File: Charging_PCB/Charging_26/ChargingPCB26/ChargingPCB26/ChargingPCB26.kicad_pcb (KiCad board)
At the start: 2 copper layers, 100 x 100 mm, 61 parts, among them J1 Molex6pin, J2 Molex6pin, K101 Relay_SPDT_Omron_G2RL-1, K102 Relay_SPDT_Omron_G2RL-1, Q1 Q_NMOS_GDS, Q103 Q_NPN_BEC, Q104 Q_NPN_BEC, Q105 Q_NPN_BEC, Q106 Q_NPN_BEC, Q2 Q_NMOS_GDS, Q3 Q_NMOS_GDS, Q4 Q_NMOS_GDS, SW101 SW_Omron_B3FS, SW102 SW_Omron_B3FS, U1 SFH617A-1, U107 LM7805_TO220, U2 SFH617A-1, U5 74LS279, U6 74HC00

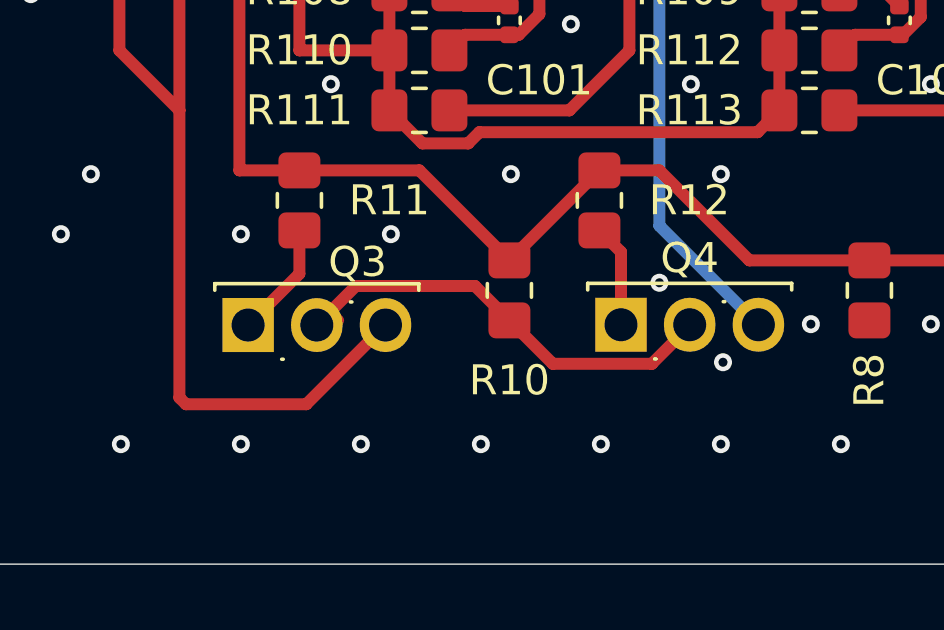
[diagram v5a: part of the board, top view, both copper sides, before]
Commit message: charging
fixed issue where Q3 and Q4 mosfets had source and drain swapped
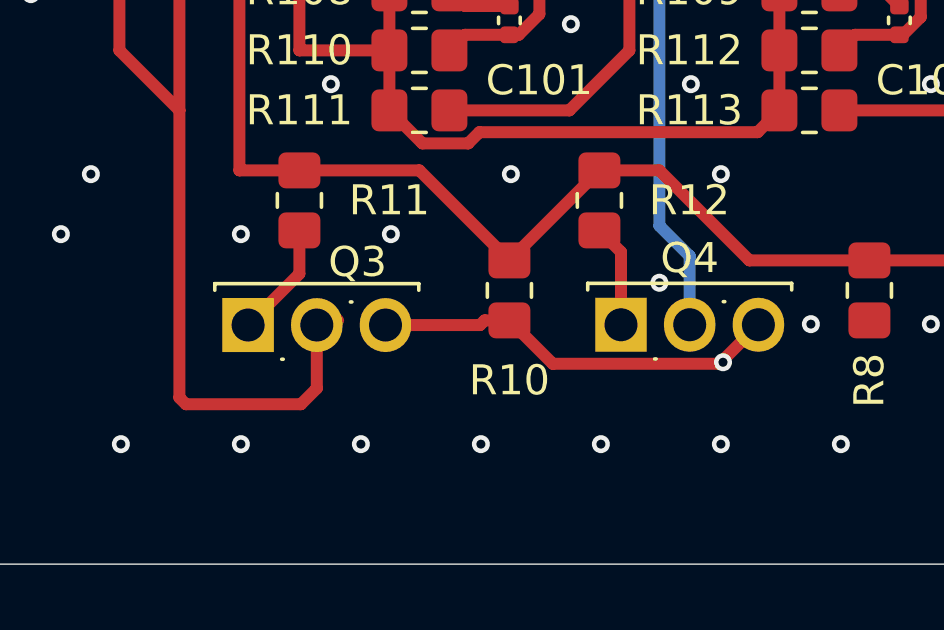
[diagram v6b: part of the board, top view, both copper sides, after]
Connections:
- Q3 pad 2: GND -> /-12V_Contactor
- Q3 pad 3: /-12V_Contactor -> GND
- Q4 pad 2: GND -> Net-(D3-K)
- Q4 pad 3: Net-(D3-K) -> GND
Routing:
- net GND: track 20.3 -> 18.6 mm
- net /-12V_Contactor: track 104.1 -> 103.4 mm
- net Net-(D3-K): track 63.8 -> 63.2 mm
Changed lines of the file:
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@@
 			(layers "*.Cu" "*.Mask")
 			(remove_unused_layers no)
-			(net 2 "GND")
+			(net 12 "Net-(D3-K)")
 			(pinfunction "D")
 			(pintype "passive")
@@
 			(layers "*.Cu" "*.Mask")
 			(remove_unused_layers no)
-			(net 12 "Net-(D3-K)")
+			(net 2 "GND")
 			(pinfunction "S")
 			(pintype "passive")
@@
 			(layers "*.Cu" "*.Mask")
 			(remove_unused_layers no)
-			(net 2 "GND")
+			(net 41 "/-12V_Contactor")
 			(pinfunction "D")
 			(pintype "passive")
@@
 			(layers "*.Cu" "*.Mask")
 			(remove_unused_layers no)
-			(net 41 "/-12V_Contactor")
+			(net 2 "GND")
 			(pinfunction "S")
 			(pintype "passive")
@@
 	)
 	(segment
-		(start 79.96 142.02)
-		(end 79.96 142.06125)
-		(width 0.4)
-		(layer "F.Cu")
-		(net 2)
-	)
-	(segment
-		(start 78.70025 143.321)
-		(end 75.396 143.321)
+		(start 75.396 143.321)
+		(end 80.949 143.321)
 		(width 0.4)
 		(layer "F.Cu")
@@
 	)
 	(segment
-		(start 68.831 140.729)
-		(end 72.804 140.729)
-		(width 0.4)
-		(layer "F.Cu")
-		(net 2)
-	)
-	(segment
-		(start 75.396 143.321)
-		(end 73.95 141.875)
+		(start 73.125 141.875)
+		(end 72.97 142.03)
 		(width 0.4)
 		(layer "F.Cu")
@@
 	)
 	(segment
-		(start 79.95 141.60425)
-		(end 79.95 141.875)
+		(start 73.95 141.875)
+		(end 73.125 141.875)
 		(width 0.4)
 		(layer "F.Cu")
@@
 	)
 	(segment
-		(start 79.96 142.06125)
-		(end 78.70025 143.321)
+		(start 72.97 142.03)
+		(end 69.82 142.03)
 		(width 0.4)
 		(layer "F.Cu")
@@
 	)
 	(segment
-		(start 72.804 140.729)
-		(end 73.95 141.875)
+		(start 80.949 143.321)
+		(end 82.25 142.02)
 		(width 0.4)
 		(layer "F.Cu")
@@
 	)
 	(segment
-		(start 67.95 141.585)
-		(end 68.24 141.875)
-		(width 0.4)
-		(layer "F.Cu")
-		(net 2)
-	)
-	(segment
-		(start 67.53 142.03)
-		(end 68.831 140.729)
+		(start 73.95 141.875)
+		(end 75.396 143.321)
 		(width 0.4)
 		(layer "F.Cu")
@@
 	)
 	(segment
+		(start 79.96 142.02)
+		(end 79.96 142.06125)
+		(width 0.4)
+		(layer "F.Cu")
+		(net 12)
+	)
+	(segment
+		(start 79.95 141.60425)
+		(end 79.95 141.875)
+		(width 0.4)
+		(layer "F.Cu")
+		(net 12)
+	)
+	(segment
 		(start 63.95 89.875)
 		(end 64.2 90.125)
@@
 	)
 	(segment
-		(start 78.95 138.72)
-		(end 82.25 142.02)
+		(start 79.96 142.02)
+		(end 79.96 139.73)
 		(width 0.4)
 		(layer "B.Cu")
@@
 	)
 	(segment
+		(start 79.96 139.73)
+		(end 78.95 138.72)
+		(width 0.4)
+		(layer "B.Cu")
+		(net 12)
+	)
+	(segment
 		(start 78.95 112.875)
 		(end 78.95 138.72)
@@
 	)
 	(segment
+		(start 62.95 144.45)
+		(end 63.17 144.67)
+		(width 0.4)
+		(layer "F.Cu")
+		(net 41)
+	)
+	(segment
 		(start 60.95 132.875)
 		(end 62.95 134.875)
@@
 	)
 	(segment
-		(start 62.95 134.875)
-		(end 62.95 144.45)
+		(start 67.53 144.14)
+		(end 67.53 142.03)
 		(width 0.4)
 		(layer "F.Cu")
@@
 	)
 	(segment
-		(start 67.18 144.67)
-		(end 69.82 142.03)
+		(start 63.17 144.67)
+		(end 67 144.67)
 		(width 0.4)
 		(layer "F.Cu")
@@
 	)
 	(segment
-		(start 62.95 129.875)
-		(end 62.95 134.875)
+		(start 67 144.67)
+		(end 67.53 144.14)
 		(width 0.4)
 		(layer "F.Cu")
@@
 	)
 	(segment
-		(start 63.17 144.67)
-		(end 67.18 144.67)
+		(start 62.95 129.875)
+		(end 62.95 134.875)
 		(width 0.4)
 		(layer "F.Cu")
@@
 	)
 	(segment
-		(start 60.95 132.875)
-		(end 60.95 69.875)
+		(start 62.95 134.875)
+		(end 62.95 144.45)
 		(width 0.4)
 		(layer "F.Cu")
@@
 	)
 	(segment
-		(start 60.95 69.875)
-		(end 69.765058 69.875)
+		(start 67.95 141.585)
+		(end 68.24 141.875)
 		(width 0.4)
 		(layer "F.Cu")
@@
 	)
 	(segment
-		(start 62.95 144.45)
-		(end 63.17 144.67)
+		(start 60.95 132.875)
+		(end 60.95 69.875)
+		(width 0.4)
+		(layer "F.Cu")
+		(net 41)
+	)
+	(segment
+		(start 60.95 69.875)
+		(end 69.765058 69.875)
 		(width 0.4)
 		(layer "F.Cu")
